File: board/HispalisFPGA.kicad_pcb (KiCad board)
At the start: 2 copper layers, 112 parts, among them Q1 DMG1012T, Q2 DMG1012T, Q3 DMG1012T, Q4 DMG1012T, SW1 SW_DIP_x08

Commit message: Set manufacturer constraints and track widths
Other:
- copper layers 2 -> 4
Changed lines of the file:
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@@
 	(layers
 		(0 "F.Cu" signal)
+		(1 "In1.Cu" power)
+		(2 "In2.Cu" power)
 		(31 "B.Cu" signal)
 		(32 "B.Adhes" user "B.Adhesive")
@@
 	)
 	(setup
+		(stackup
+			(layer "F.SilkS"
+				(type "Top Silk Screen")
+			)
+			(layer "F.Paste"
+				(type "Top Solder Paste")
+			)
+			(layer "F.Mask"
+				(type "Top Solder Mask")
+				(thickness 0.01)
+			)
+			(layer "F.Cu"
+				(type "copper")
+				(thickness 0.035)
+			)
+			(layer "dielectric 1"
+				(type "prepreg")
+				(thickness 0.1)
+				(material "FR4")
+				(epsilon_r 4.5)
+				(loss_tangent 0.02)
+			)
+			(layer "In1.Cu"
+				(type "copper")
+				(thickness 0.035)
+			)
+			(layer "dielectric 2"
+				(type "core")
+				(thickness 1.24)
+				(material "FR4")
+				(epsilon_r 4.5)
+				(loss_tangent 0.02)
+			)
+			(layer "In2.Cu"
+				(type "copper")
+				(thickness 0.035)
+			)
+			(layer "dielectric 3"
+				(type "prepreg")
+				(thickness 0.1)
+				(material "FR4")
+				(epsilon_r 4.5)
+				(loss_tangent 0.02)
+			)
+			(layer "B.Cu"
+				(type "copper")
+				(thickness 0.035)
+			)
+			(layer "B.Mask"
+				(type "Bottom Solder Mask")
+				(thickness 0.01)
+			)
+			(layer "B.Paste"
+				(type "Bottom Solder Paste")
+			)
+			(layer "B.SilkS"
+				(type "Bottom Silk Screen")
+			)
+			(copper_finish "None")
+			(dielectric_constraints no)
+		)
 		(pad_to_mask_clearance 0)
 		(allow_soldermask_bridges_in_footprints no)

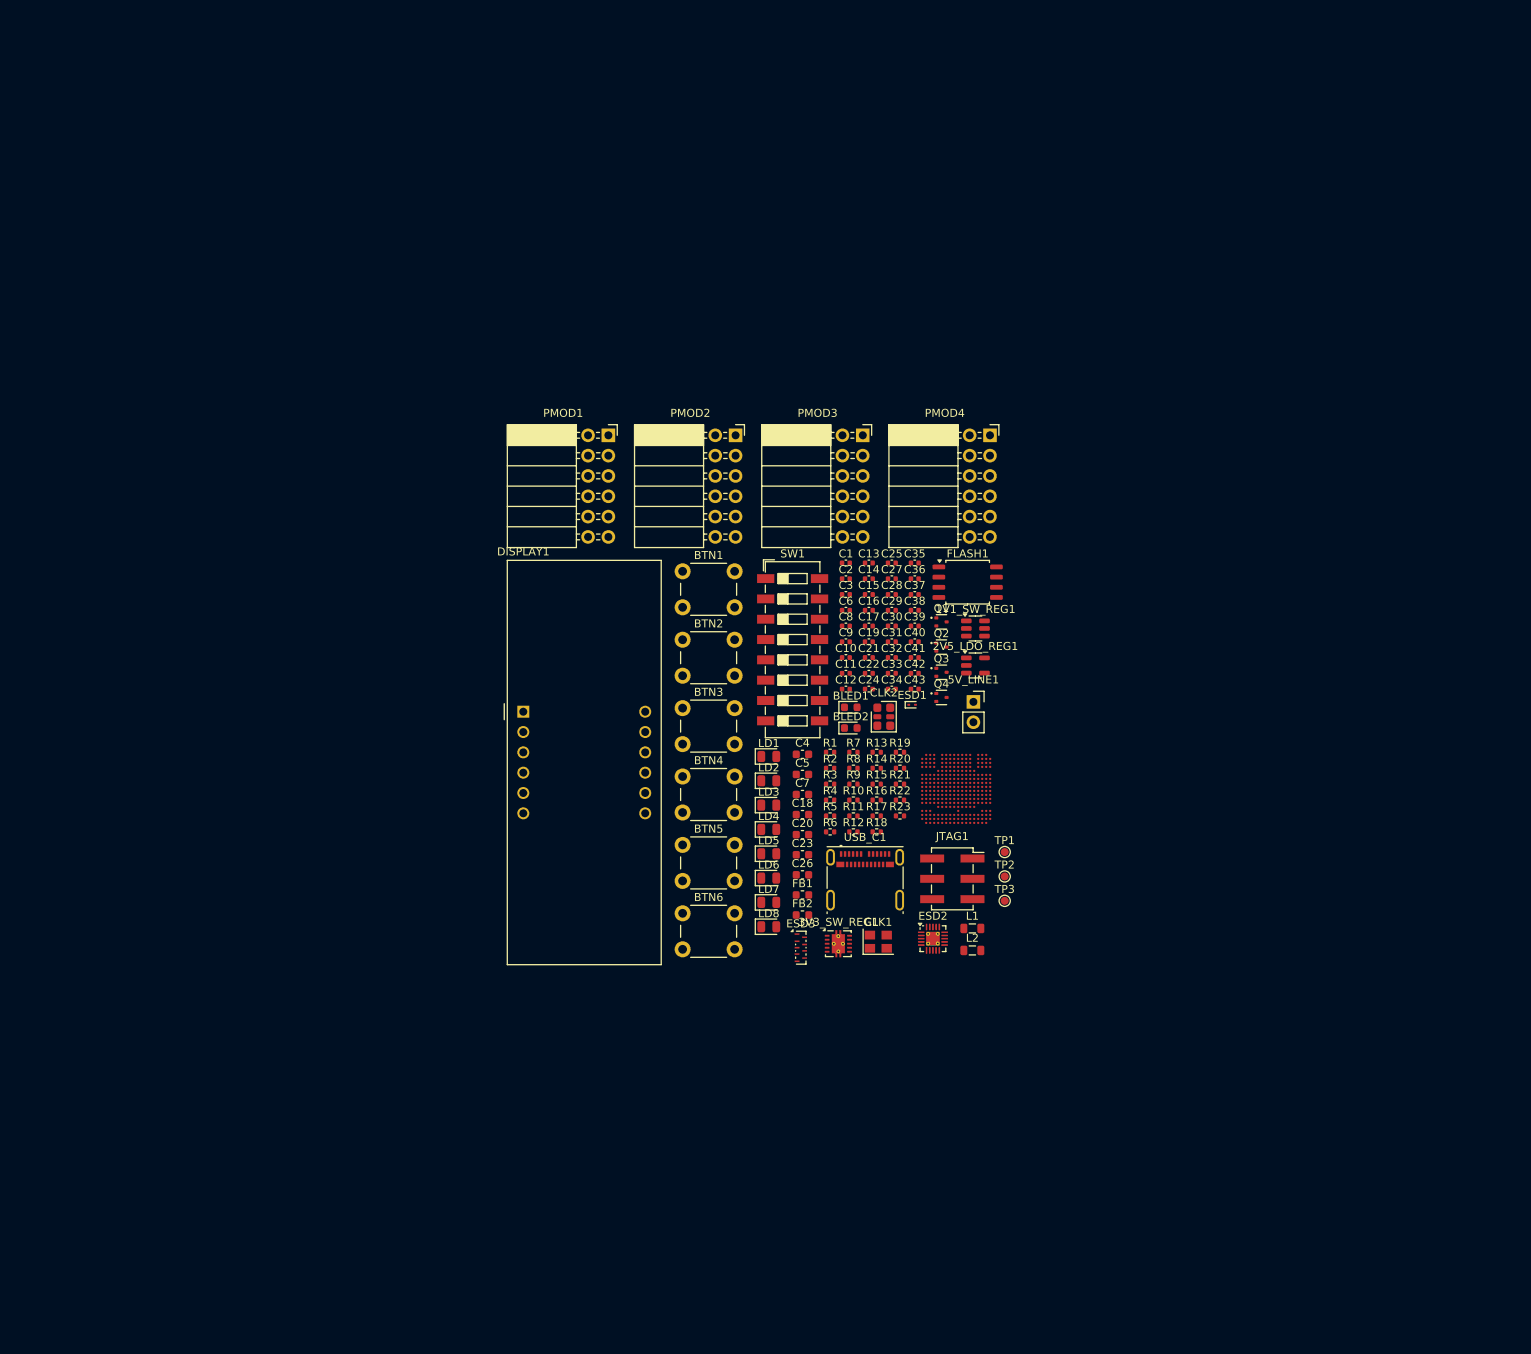
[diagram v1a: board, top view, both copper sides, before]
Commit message: Final connection of ECP5 chip
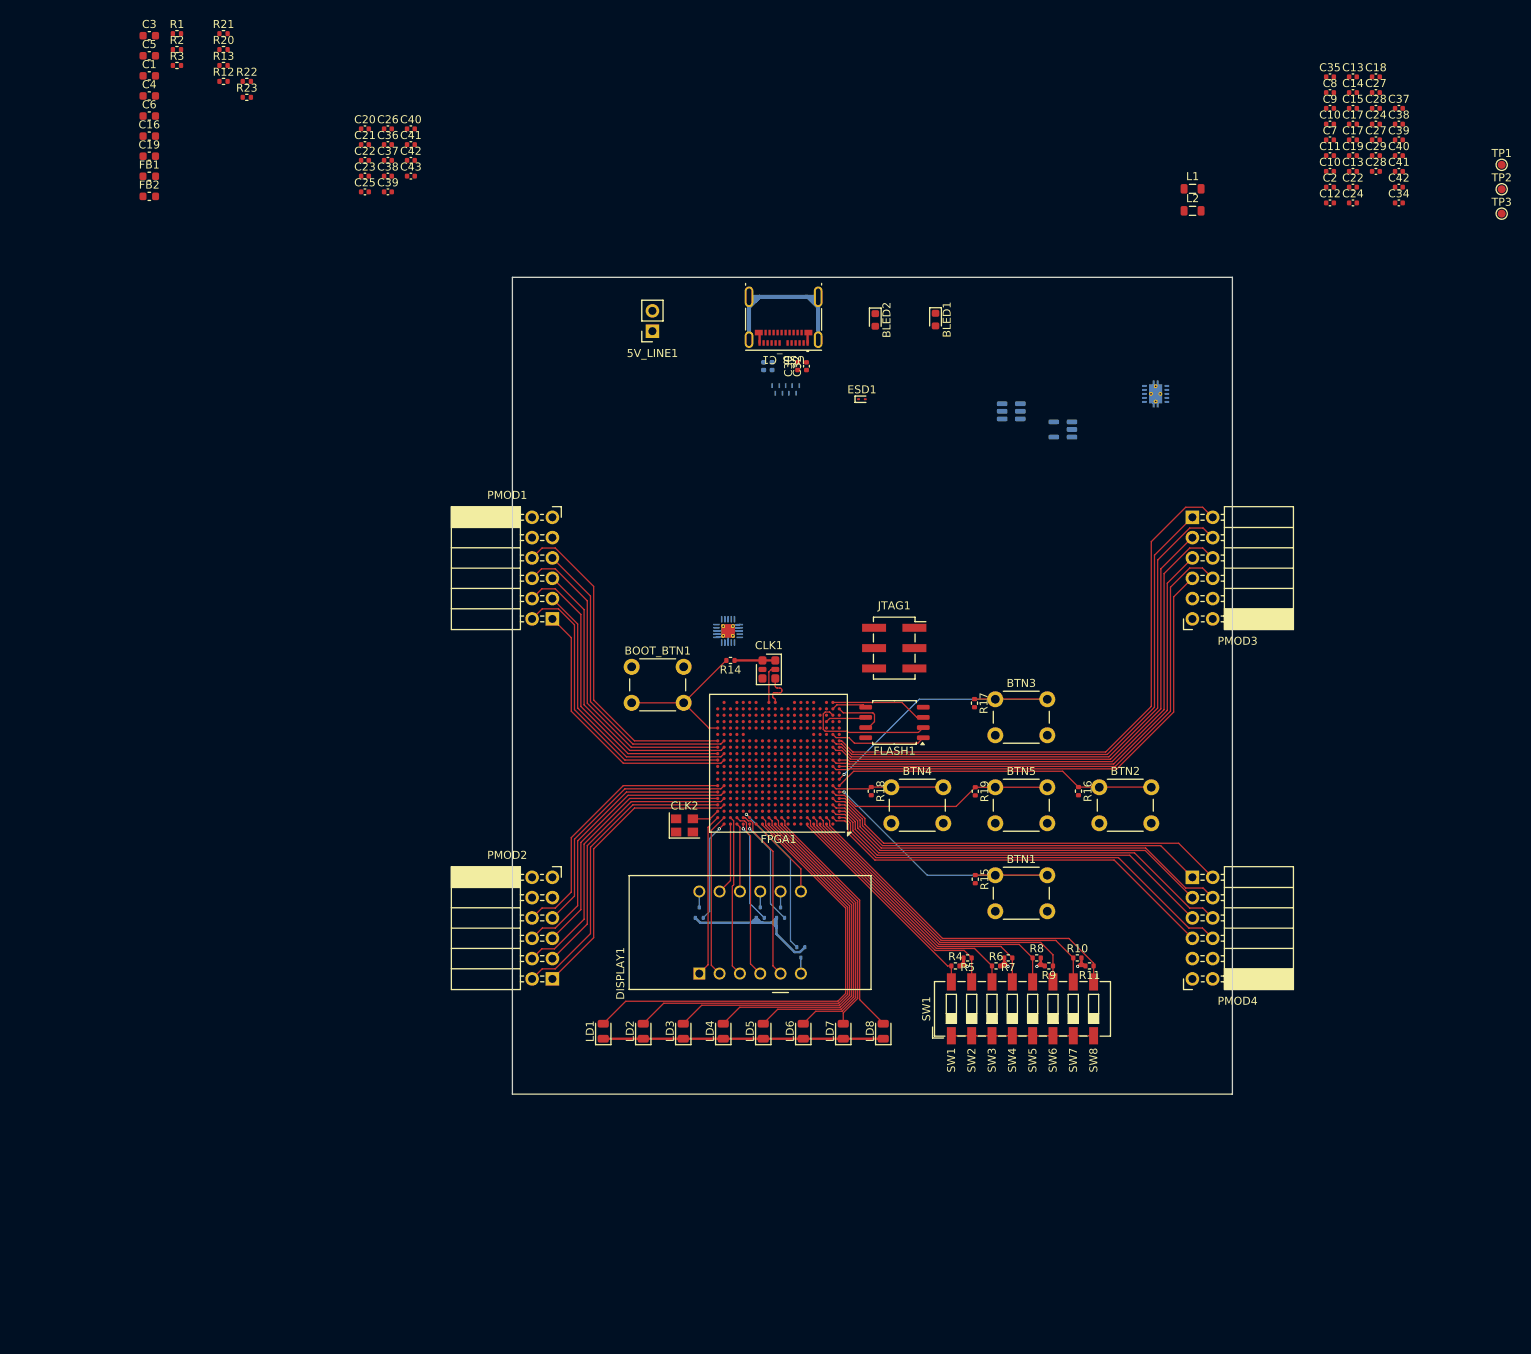
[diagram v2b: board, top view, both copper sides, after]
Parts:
- removed the BTN5 at (135.7, 121.8)
- added BTN4: SW_Push, Button_Switch_THT:SW_PUSH_6mm, F.Cu at (161.8, 114.6)
- added C20: 100nF, Capacitor_SMD:C_0402_1005Metric, F.Cu at (96.0, 32.3)
- added C21: 10nF, Capacitor_SMD:C_0402_1005Metric, F.Cu at (96.0, 34.3)
- added C22: 100nF, Capacitor_SMD:C_0402_1005Metric, F.Cu at (96.0, 36.2)
- added C23: 10nF, Capacitor_SMD:C_0402_1005Metric, F.Cu at (96.0, 38.2)
- added C25: 1nF, Capacitor_SMD:C_0402_1005Metric, F.Cu at (96.0, 40.2)
- added C26: 1nF, Capacitor_SMD:C_0402_1005Metric, F.Cu at (98.9, 32.3)
- added C36: 100nF, Capacitor_SMD:C_0402_1005Metric, F.Cu at (98.9, 34.3)
- added C37: 10nF, Capacitor_SMD:C_0402_1005Metric, F.Cu at (98.9, 36.2)
- added C38: 100nF, Capacitor_SMD:C_0402_1005Metric, F.Cu at (98.9, 38.2)
- added C39: 10nF, Capacitor_SMD:C_0402_1005Metric, F.Cu at (98.9, 40.2)
- added C40: 100nF, Capacitor_SMD:C_0402_1005Metric, F.Cu at (101.8, 32.3)
- added C41: 10nF, Capacitor_SMD:C_0402_1005Metric, F.Cu at (101.8, 34.3)
- added C42: 100nF, Capacitor_SMD:C_0402_1005Metric, F.Cu at (101.8, 36.2)
- added C43: 10nF, Capacitor_SMD:C_0402_1005Metric, F.Cu at (101.8, 38.2)
- C31: renamed from C34; moved to B.Cu
- C33: renamed from C36; moved to B.Cu
- DISPLAY1: footprint Display_7Segment:CA56-12SRWA -> HispalisFPGA:MHDC3641SRBW
- ESD2, ESD3, Q1, Q2, Q3, Q4: moved to B.Cu
- FPGA1: value LFE5UM-285 -> LFE5UM-381; footprint Footprints:csfBGA 285 -> Package_BGA:Lattice_caBGA-381_17.0x17.0mm_Layout20x20_P0.8mm_Ball0.4mm_Pad0.4mm_NSMD
- LDO_REG1: renamed from 2V5_LDO_REG1; moved to B.Cu
- PMOD1, PMOD2, PMOD3, PMOD4: footprint Connector_PinSocket_2.54mm:PinSocket_2x06_P2.54mm_Horizontal -> HispalisFPGA:PMOD_Socket_Horizontal
- SW_REG1: renamed from 3V3_SW_REG1; moved to B.Cu
- SW_REG2: renamed from 1V1_SW_REG1; moved to B.Cu
- moved C1 121.4 mm to (69.0, 25.7)
- moved C16 121.4 mm to (69.0, 33.2)
- moved FB1 121.4 mm to (69.0, 38.2)
- moved R1 121.4 mm to (72.5, 20.4)
- moved R21 121.4 mm to (78.3, 20.4)
- moved C19 121.4 mm to (69.0, 35.7)
- moved C3 121.4 mm to (69.0, 20.7)
- moved C4 121.4 mm to (69.0, 28.2)
- moved C5 121.4 mm to (69.0, 23.2)
- moved C6 121.4 mm to (69.0, 30.7)
- moved FB2 121.4 mm to (69.0, 40.7)
- moved R12 121.4 mm to (78.3, 26.4)
- moved R13 121.4 mm to (78.3, 24.4)
- moved R2 121.4 mm to (72.5, 22.4)
- moved R20 121.4 mm to (78.3, 22.4)
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- renumbered BLED2 to BLED1, BLED1 to BLED2, BTN1 to BOOT_BTN1, BTN2 to BTN1, BTN3 to BTN2, BTN4 to BTN3, BTN6 to BTN5, C7 to C1, C6 to C10, C9 to C11, C21 to C13, C23 to C16, C16 to C17, C25 to C18, C26 to C19, C11 to C2, C29 to C24, C30 to C27, C32 to C28, C31 to C29, C4 to C3, C33 to C30, C35 to C32, C43 to C34, C1 to C35, C18 to C4, C20 to C6, C8 to C7, C2 to C8, C3 to C9, CLK2 to CLK1, CLK1 to CLK2, R16 to R12, R15 to R13, R12 to R14, R17 to R15, R18 to R16, R19 to R17, R20 to R18, R21 to R19, R14 to R20, R13 to R21
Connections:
- BTN1 pad 2: VCCIO0 -> +3V3
- BTN2 pad 2: VCCIO0 -> +3V3
- BTN3 pad 2: VCCIO0 -> +3V3
- BTN5 pad 2: VCCIO0 -> +3V3
- C10 pad 1: FPGA_PWR -> +1V1
- C11 pad 1: FPGA_PWR -> +1V1
- C12 pad 1: FPGA_PWR -> +1V1
- C14 pad 1: FPGA_PWR -> +1V1
- C15 pad 1: FPGA_PWR -> +1V1
- C16 pad 1: FPGA_PWR -> +1V1
- C17 pad 1: FPGA_PWR -> +1V1
- C19 pad 1: FPGA_PWR -> +1V1
- C27 pad 1: VCCIO0 -> +3V3
- C28 pad 1: VCCIO0 -> +3V3
- C35 pad 1: VCCIO0 -> +3V3
- C4 pad 1: VCCIO0 -> +3V3
- C6 pad 1: VCCIO0 -> +3V3
- CLK1 pad 1: VCCIO0 -> +3V3
- CLK1 pad 4: USB3_REFCLK_P -> Net-(CLK1-OUT+)
- CLK1 pad 5: USB3_REFCLK_N -> Net-(CLK1-OUT-)
- CLK1 pad 6: VCCIO0 -> +3V3
- CLK2 pad 1: VCCIO0 -> +3V3
- CLK2 pad 4: VCCIO0 -> +3V3
- DISPLAY1 pad 1: DISPLAY_CE -> DISPLAY_SE
- DISPLAY1 pad 10: DISPLAY_CF -> DISPLAY_SF
- DISPLAY1 pad 11: DISPLAY_CA -> DISPLAY_SA
- DISPLAY1 pad 2: DISPLAY_CD -> DISPLAY_SD
- DISPLAY1 pad 3: DISPLAY_CDP -> DISPLAY_SDP
- DISPLAY1 pad 4: DISPLAY_CC -> DISPLAY_SC
- DISPLAY1 pad 5: DISPLAY_CG -> DISPLAY_SG
- DISPLAY1 pad 7: DISPLAY_CB -> DISPLAY_SB
- ESD2 pad 10: +3.3V -> +3V3
- FLASH1 pad 8: VCCIO0 -> +3V3
- FPGA1 pad A10: unconnected-(FPGA1A-PT27AB-/PCLKC0_1-PadA10) -> LED7
- FPGA1 pad A11: PMOD3_3 -> LED5
- FPGA1 pad A12: PMOD3_7 -> LED3
- FPGA1 pad A13: PMOD2_9 -> LED1
- FPGA1 pad A15: PMOD2_8 -> DISPLAY_D3
- FPGA1 pad A16: PMOD2_4 -> DISPLAY_D2
- FPGA1 pad A17: PMOD2_3 -> DISPLAY_SF
- FPGA1 pad A2: BTN1 -> unconnected-(FPGA1G-PL35A-PadA2)
- FPGA1 pad A3: PMOD4_3 -> SW7
- FPGA1 pad A4: unconnected-(FPGA1C-PR11AB--PadA4) -> SW5
- FPGA1 pad A6: SW7 -> SW1
- FPGA1 pad A7: SW8 -> unconnected-(FPGA1B-PT18A-PadA7)
- FPGA1 pad B1: PMOD4_2 -> PMOD4_10
- FPGA1 pad B10: unconnected-(FPGA1A-PT29AB+/PCLKT0_0-PadB10) -> LED8
- FPGA1 pad B11: PMOD3_4 -> LED6
- FPGA1 pad B12: PMOD3_8 -> LED4
- FPGA1 pad B13: PMOD2_10 -> LED2
- FPGA1 pad B15: PMOD2_7 -> DISPLAY_D4
- FPGA1 pad B16: GND -> DISPLAY_SG
- FPGA1 pad B17: CLK_16MHz -> DISPLAY_SC
- FPGA1 pad B18: PMOD2_2 -> DISPLAY_SDP
- FPGA1 pad B2: BTN2 -> PMOD4_4
- FPGA1 pad B3: GND -> SW8
- FPGA1 pad B4: BTN3 -> SW6
- FPGA1 pad B6: SW6 -> SW2
- FPGA1 pad B7: PMOD3_10 -> GND
- FPGA1 pad B8: PMOD3_9 -> unconnected-(FPGA1B-PT15B-PadB8)
- FPGA1 pad C1: PMOD4_7 -> PMOD4_9
- FPGA1 pad C12: STATUS_LED -> unconnected-(FPGA1C-PT71B-PadC12)
- FPGA1 pad C15: PMOD3_2 -> unconnected-(FPGA1C-PT105B-PadC15)
- FPGA1 pad C16: USB_CONNECT -> unconnected-(FPGA1C-PT112A-PadC16)
- FPGA1 pad C17: LED8 -> unconnected-(FPGA1C-PT114B-PadC17)
- FPGA1 pad C18: SW1 -> unconnected-(FPGA1D-PR11A-PadC18)
- FPGA1 pad C2: PMOD4_4 -> PMOD4_3
- FPGA1 pad C3: SW3 -> unconnected-(FPGA1G-PL17C-PadC3)
- FPGA1 pad C4: PMOD4_1 -> unconnected-(FPGA1G-PL14A-PadC4)
- FPGA1 pad D10: FPGA_PWR -> unconnected-(FPGA1B-PT56A-PadD10)
- FPGA1 pad D11: FPGA_PWR -> unconnected-(FPGA1C-PT69A-PadD11)
- FPGA1 pad D12: VCCIO0 -> unconnected-(FPGA1C-PT74A-PadD12)
- FPGA1 pad D15: PMOD3_1 -> unconnected-(FPGA1C-PT107A-PadD15)
- FPGA1 pad D17: SW2 -> unconnected-(FPGA1D-PR11B-PadD17)
- FPGA1 pad D18: PMOD2_1 -> unconnected-(FPGA1D-PR14A-PadD18)
- FPGA1 pad D2: BTN4 -> PMOD4_2
- FPGA1 pad D3: PMOD4_9 -> unconnected-(FPGA1G-PL17D-PadD3)
- FPGA1 pad D4: unconnected-(FPGA1C-PR14AB+-PadD4) -> GND
- FPGA1 pad D7: VCCIO0 -> unconnected-(FPGA1B-PT9B-PadD7)
- FPGA1 pad D8: FPGA_PWR -> unconnected-(FPGA1B-PT13B-PadD8)
- FPGA1 pad D9: FPGA_PWR -> unconnected-(FPGA1B-PT20A-PadD9)
- FPGA1 pad E10: GND -> unconnected-(FPGA1B-PT56B-PadE10)
- FPGA1 pad E11: GND -> unconnected-(FPGA1C-PT69B-PadE11)
- FPGA1 pad E12: GND -> unconnected-(FPGA1C-PT74B-PadE12)
- FPGA1 pad E13: +2V5 -> unconnected-(FPGA1C-PT80B-PadE13)
- FPGA1 pad E14: GND -> unconnected-(FPGA1C-PT85B-PadE14)
- FPGA1 pad E5: GND -> unconnected-(FPGA1G-PL20C-PadE5)
- FPGA1 pad E6: +2V5 -> unconnected-(FPGA1B-PT6A-PadE6)
- FPGA1 pad E7: GND -> unconnected-(FPGA1B-PT9A-PadE7)
- FPGA1 pad E8: GND -> unconnected-(FPGA1B-PT13A-PadE8)
- FPGA1 pad E9: GND -> unconnected-(FPGA1B-PT20B-PadE9)
- FPGA1 pad F1: unconnected-(FPGA1D-PR35CD+-PadF1) -> BTN1
- FPGA1 pad F10: GND -> +3V3
- FPGA1 pad F11: GND -> +3V3
- FPGA1 pad F12: GND -> +3V3
- FPGA1 pad F15: unconnected-(FPGA1E-PL29CD+/GR_PCLK6_1-PadF15) -> +2V5
- FPGA1 pad F16: USB_D- -> unconnected-(FPGA1D-PR11D-PadF16)
- FPGA1 pad F17: USB_D+ -> unconnected-(FPGA1D-PR17A-PadF17)
- FPGA1 pad F18: PMOD1_1 -> unconnected-(FPGA1D-PR14D-PadF18)
- FPGA1 pad F2: unconnected-(FPGA1D-PR32AB+/RDQS32-PadF2) -> BTN5
- FPGA1 pad F4: SW4 -> unconnected-(FPGA1G-PL20A-PadF4)
- FPGA1 pad F5: GND -> unconnected-(FPGA1G-PL20D-PadF5)
- FPGA1 pad F6: GND -> +2V5
- FPGA1 pad F9: GND -> +3V3
- FPGA1 pad G1: unconnected-(FPGA1D-PR32AB-/RDQSN32-PadG1) -> BTN2
- FPGA1 pad G14: VCCIO0 -> GND
- FPGA1 pad G15: unconnected-(FPGA1E-PL35AB+-PadG15) -> GND
- FPGA1 pad G18: PMOD1_10 -> unconnected-(FPGA1D-PR17B-PadG18)
- FPGA1 pad G2: GND -> BTN4
- FPGA1 pad G4: unconnected-(FPGA1D-PR26AB-/PCLKC3_1-PadG4) -> GND
- FPGA1 pad G5: VCCIO0 -> unconnected-(FPGA1G-PL41B-PadG5)
- FPGA1 pad H1: unconnected-(FPGA1D-PR35CD--PadH1) -> BTN3
- FPGA1 pad H10: GND -> +1V1
- FPGA1 pad H11: GND -> +1V1
- FPGA1 pad H12: GND -> +1V1
- FPGA1 pad H13: GND -> +1V1
- FPGA1 pad H14: VCCIO0 -> +3V3
- FPGA1 pad H15: unconnected-(FPGA1E-PL35AB--PadH15) -> +3V3
- FPGA1 pad H17: PMOD1_2 -> unconnected-(FPGA1D-PR20B-PadH17)
- FPGA1 pad H18: PMOD1_3 -> unconnected-(FPGA1D-PR20A-PadH18)
- FPGA1 pad H5: VCCIO0 -> unconnected-(FPGA1G-PL41C-PadH5)
- FPGA1 pad H6: GND -> +3V3
- FPGA1 pad H7: GND -> +3V3
- FPGA1 pad H8: GND -> +1V1
- FPGA1 pad H9: GND -> +1V1
- FPGA1 pad J13: GND -> +1V1
- FPGA1 pad J14: FPGA_PWR -> GND
- FPGA1 pad J15: FPGA_PWR -> +3V3
- FPGA1 pad J17: PMOD1_4 -> unconnected-(FPGA1D-PR20C-PadJ17)
- FPGA1 pad J18: LED3 -> unconnected-(FPGA1D-PR41C-PadJ18)
- FPGA1 pad J2: unconnected-(FPGA1D-PR35AB+-PadJ2) -> GND
- FPGA1 pad J4: FPGA_PWR -> unconnected-(FPGA1F-PL50A-PadJ4)
- FPGA1 pad J5: FPGA_PWR -> unconnected-(FPGA1F-PL50B-PadJ5)
- FPGA1 pad J6: GND -> +3V3
- FPGA1 pad J8: GND -> +1V1
- FPGA1 pad K1: unconnected-(FPGA1D-PR41CD--PadK1) -> PMOD3_10
- FPGA1 pad K13: GND -> +1V1
- FPGA1 pad K15: unconnected-(FPGA1E-PL41CD--PadK15) -> GND
- FPGA1 pad K17: LED4 -> unconnected-(FPGA1D-PR29B-PadK17)
- FPGA1 pad K18: LED5 -> unconnected-(FPGA1D-PR41D-PadK18)
- FPGA1 pad K2: unconnected-(FPGA1D-PR44AB+/RDQS44-PadK2) -> PMOD3_4
- FPGA1 pad K5: GND -> unconnected-(FPGA1F-PL56B-PadK5)
- FPGA1 pad K8: GND -> +1V1
- FPGA1 pad L1: unconnected-(FPGA1D-PR44AB-/RDQSN44-PadL1) -> PMOD3_9
- FPGA1 pad L13: GND -> +1V1
- FPGA1 pad L14: GND -> +3V3
- FPGA1 pad L15: unconnected-(FPGA1E-PL44CD+-PadL15) -> +3V3
- FPGA1 pad L17: GND -> unconnected-(FPGA1E-PR50B-PadL17)
- FPGA1 pad L18: LED6 -> unconnected-(FPGA1E-PR50C-PadL18)
- FPGA1 pad L2: GND -> PMOD3_3
- FPGA1 pad L5: GND -> unconnected-(FPGA1F-PL56D-PadL5)
- FPGA1 pad L6: GND -> +3V3
- FPGA1 pad L7: GND -> +3V3
- FPGA1 pad L8: GND -> +1V1
- FPGA1 pad M13: GND -> +1V1
- FPGA1 pad M14: VCCIO0 -> GND
- FPGA1 pad M15: FPGA_PWR -> +3V3
- FPGA1 pad M16: unconnected-(FPGA1E-PL47CD+/LLC_GPLL0T_IN-PadM16) -> GND
- FPGA1 pad M17: PMOD1_9 -> unconnected-(FPGA1E-PR53B-PadM17)
- FPGA1 pad M18: PMOD1_8 -> unconnected-(FPGA1E-PR50D-PadM18)
- FPGA1 pad M2: unconnected-(FPGA1D-PR44CD+-PadM2) -> GND
- FPGA1 pad M3: unconnected-(FPGA1D-PR41AB+-PadM3) -> USB_D-
- FPGA1 pad M4: FPGA_PWR -> unconnected-(FPGA1F-PL83A-PadM4)
- FPGA1 pad M5: VCCIO0 -> unconnected-(FPGA1F-PL77A-PadM5)
- FPGA1 pad M6: GND -> +3V3
- FPGA1 pad M8: GND -> +1V1
- FPGA1 pad N1: unconnected-(FPGA1D-PR47CD-/LRC_GPLL0C_IN-PadN1) -> PMOD3_8
- FPGA1 pad N10: GND -> +1V1
- FPGA1 pad N11: GND -> +1V1
- FPGA1 pad N12: GND -> +1V1
- FPGA1 pad N13: VCCIO0 -> +1V1
- FPGA1 pad N14: VCCIO0 -> GND
- FPGA1 pad N15: unconnected-(FPGA1G-PB4AB+-PadN15) -> GND
- FPGA1 pad N16: LED7 -> unconnected-(FPGA1E-PR53A-PadN16)
- FPGA1 pad N17: PMOD1_7 -> unconnected-(FPGA1E-PR56A-PadN17)
- FPGA1 pad N18: IO3 -> unconnected-(FPGA1E-PR53C-PadN18)
- FPGA1 pad N2: unconnected-(FPGA1D-PR44CD--PadN2) -> PMOD3_2
- FPGA1 pad N3: BTN5 -> USB_D+
- FPGA1 pad N4: SW5 -> unconnected-(FPGA1F-PL83C-PadN4)
- FPGA1 pad N5: VCCIO0 -> unconnected-(FPGA1F-PL83B-PadN5)
- FPGA1 pad N6: +2V5 -> GND
- FPGA1 pad N8: GND -> +1V1
- FPGA1 pad N9: GND -> +1V1
- FPGA1 pad P10: FPGA_PWR -> +3V3
- FPGA1 pad P11: FPGA_PWR -> GND
- FPGA1 pad P13: +2V5 -> GND
- FPGA1 pad P14: VCCIO0 -> GND
- FPGA1 pad P5: +2V5 -> USB_CONNECT
- FPGA1 pad P6: GND -> +2V5
- FPGA1 pad P7: FPGA_PWR -> GND
- FPGA1 pad P9: FPGA_PWR -> +3V3
- FPGA1 pad R1: GND -> unconnected-(FPGA1H-PB4A-PadR1)
- FPGA1 pad R16: LED2 -> unconnected-(FPGA1E-PR56C-PadR16)
- FPGA1 pad R17: PMOD4_10 -> unconnected-(FPGA1E-PR56D-PadR17)
- FPGA1 pad R18: IO2 -> unconnected-(FPGA1E-PR89B-PadR18)
- FPGA1 pad R2: GND -> CSSPIN
- FPGA1 pad R3: +2V5 -> unconnected-(FPGA1H-PB15B-PadR3)
- FPGA1 pad T1: USB3_REFCLK_N -> unconnected-(FPGA1H-PB4B-PadT1)
- FPGA1 pad T10: GND -> +1V1
- FPGA1 pad T11: GND -> +1V1
- FPGA1 pad T12: GND -> +1V1
- FPGA1 pad T13: TDI -> +1V1
- FPGA1 pad T14: CFG_MODE_SEL_1 -> +1V1
- FPGA1 pad T15: PROGRAMN -> +1V1
- FPGA1 pad T16: GND -> unconnected-(FPGA1E-PR77A-PadT16)
- FPGA1 pad T17: PROGRAMN -> unconnected-(FPGA1E-PR92D-PadT17)
- FPGA1 pad T18: MISO -> unconnected-(FPGA1E-PR89D-PadT18)
- FPGA1 pad T2: GND -> unconnected-(FPGA1H-PB13A-PadT2)
- FPGA1 pad T3: GND -> unconnected-(FPGA1H-PB18A-PadT3)
- FPGA1 pad T4: GND -> Net-(FPGA1I-CFG_1)
- FPGA1 pad T5: FPGA_PWR -> TCK
- FPGA1 pad T6: GND -> +1V1
- FPGA1 pad T7: GND -> +1V1
- FPGA1 pad T8: GND -> +1V1
- FPGA1 pad T9: GND -> +1V1
- FPGA1 pad U1: USB3_REFCLK_P -> unconnected-(FPGA1H-PB6A-PadU1)
- FPGA1 pad U12: FPGA_PWR -> GND
- FPGA1 pad U13: TCK -> GND
- FPGA1 pad U14: CFG_MODE_SEL_0 -> GND
- FPGA1 pad U15: DONE -> +1V1
- FPGA1 pad U16: SCK -> unconnected-(FPGA1E-PR92C-PadU16)
- FPGA1 pad U17: CSSPIN -> CC2
- FPGA1 pad U18: MOSI -> CC1
- FPGA1 pad U2: GND -> unconnected-(FPGA1H-PB13B-PadU2)
- FPGA1 pad U3: GND -> SCK
- FPGA1 pad U4: GND -> Net-(FPGA1I-CFG_0)
- FPGA1 pad U5: GND -> TMS
- FPGA1 pad U6: FPGA_PWR -> +1V1
- FPGA1 pad U8: FPGA_PWR -> GND
- FPGA1 pad V10: GND -> +2V5
- FPGA1 pad V11: CH0_TX- -> +2V5
- FPGA1 pad V12: CH0_TX+ -> GND
- FPGA1 pad V13: TMS -> GND
- FPGA1 pad V14: TDO -> GND
- FPGA1 pad V15: CFG_MODE_SEL_0 -> GND
- FPGA1 pad V16: INITN -> GND
- FPGA1 pad V17: LED1 -> +2V5
- FPGA1 pad V2: CH1_TX- -> MISO
- FPGA1 pad V3: CH1_TX+ -> unconnected-(FPGA1I-~{INIT}-PadV3)
- FPGA1 pad V4: GND -> TDO
- FPGA1 pad V5: CH1_RX- -> GND
- FPGA1 pad V6: CH1_RX+ -> GND
- FPGA1 pad V8: CH0_RX- -> GND
- FPGA1 pad V9: CH0_RX+ -> GND
- JTAG1 pad 1: VCCIO0 -> +3V3
- L2 pad 2: FPGA_PWR -> +1V1
- PMOD1 pad 12: VCCIO0 -> +3V3
- PMOD1 pad 6: VCCIO0 -> +3V3
- PMOD2 pad 12: VCCIO0 -> +3V3
- PMOD2 pad 6: VCCIO0 -> +3V3
- PMOD3 pad 12: VCCIO0 -> +3V3
- PMOD3 pad 6: VCCIO0 -> +3V3
- PMOD4 pad 12: VCCIO0 -> +3V3
- PMOD4 pad 6: VCCIO0 -> +3V3
- Q1 pad 1: DISPLAY_A4 -> DISPLAY_D4
- Q2 pad 1: DISPLAY_A3 -> DISPLAY_D3
- Q3 pad 1: DISPLAY_A2 -> DISPLAY_D2
- Q4 pad 1: DISPLAY_A1 -> DISPLAY_D1
- R12 pad 1: STATUS_LED -> Net-(FPGA1I-DONE)
- R13 pad 1: VCCIO0 -> +3V3
- R14 pad 1: VCCIO0 -> +3V3
- R2 pad 1: FPGA_PWR -> +1V1
- R20 pad 1: VCCIO0 -> +3V3
- R20 pad 2: CFG_MODE_SEL_1 -> Net-(FPGA1I-CFG_1)
- R21 pad 1: CFG_MODE_SEL_0 -> Net-(FPGA1I-CFG_0)
- SW1 pad 1: SW1 -> +3V3
- SW1 pad 10: VCCIO0 -> SW7
- SW1 pad 11: VCCIO0 -> SW6
- SW1 pad 12: VCCIO0 -> SW5
- SW1 pad 13: VCCIO0 -> SW4
- SW1 pad 14: VCCIO0 -> SW3
- SW1 pad 15: VCCIO0 -> SW2
- SW1 pad 16: VCCIO0 -> SW1
- SW1 pad 2: SW2 -> +3V3
- SW1 pad 3: SW3 -> +3V3
- SW1 pad 4: SW4 -> +3V3
- SW1 pad 5: SW5 -> +3V3
- SW1 pad 6: SW6 -> +3V3
- SW1 pad 7: SW7 -> +3V3
- SW1 pad 8: SW8 -> +3V3
- SW1 pad 9: VCCIO0 -> SW8
- SW_REG1 pad 1: VCCIO0 -> +3V3
- SW_REG1 pad 10: VCCIO0 -> +3V3
- TP1 pad 1: FPGA_PWR -> +1V1
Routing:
- net GND: track 0.00 -> 83.8 mm, vias 0 -> 4
- net PMOD3_7: track 0.00 -> 72.5 mm
- net PMOD3_8: track 0.00 -> 70.4 mm
- net PMOD3_1: track 0.00 -> 69.1 mm
- net PMOD3_9: track 0.00 -> 68.3 mm
- net PMOD3_2: track 0.00 -> 67.3 mm
- net PMOD3_10: track 0.00 -> 66.6 mm
- net PMOD3_3: track 0.00 -> 65.1 mm
- net PMOD3_4: track 0.00 -> 63.4 mm
- net LED1: track 0.00 -> 57.4 mm
- net PMOD4_10: track 0.00 -> 53.6 mm
- net LED2: track 0.00 -> 53.6 mm
- net PMOD4_9: track 0.00 -> 52.8 mm
- net PMOD4_8: track 0.00 -> 52.0 mm
- net PMOD4_4: track 0.00 -> 51.9 mm
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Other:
- board outline added: 90 x 102.1 mm
- board text added: "SW1"
- board text added: "SW2"
- board text added: "SW3"
- board text added: "SW4"
- board text added: "SW5"
- board text added: "SW6"
- board text added: "SW7"
- board text added: "SW8"
